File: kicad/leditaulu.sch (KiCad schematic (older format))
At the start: 5 parts

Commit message: Continue schematic
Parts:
- added AFF1: Display 1, symbol LDS-30102BX
- added AFF2: Display 2, symbol LDS-30102BX
- added C2, C? (x2): 10uF, symbol C_Small
- added C? (x2): 1000uF, symbol C_Small
- added C?: 100uF, symbol C_Small
- added CON1: 12V input, symbol BARREL_JACK
- added P2: I2C addr select, symbol CONN_02X04
- added P?: Interconnect, symbol CONN_01X05
- added R1, R11, R2, R3, R6, R7, R8, R9: 10K, symbol R_Small
- added R10: 1K, symbol R_Small
- added U2: TLC59116IPWR, symbol TLC59116IPWR
- added U3: LD1086, SOT-223, symbol LD1117S12CTR
- gave numbers to parts that had none: 5
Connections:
- net 3V3: now also C2.2, C?.1, C?.1, C?.1, P?.2 (P2), R1.1, R11.2, R2.2, R3.2, R6.2, R7.2, R8.2, R9.2, U2.28 (VCC), U3.2 (VO); no longer U1.3 (CH_PD)
- net Earth: now also C2.1, C?.2, C?.2, C?.2, C?.2, C?.2, CON1.2, P2.1 (P1), P2.3 (P3), P2.5 (P5), P2.7 (P7), P?.5 (P5), R10.2, U2.10 (GND), U2.19 (GND), U2.24 (GND), U3.1 (GND)
- net SCL: now also P?.3 (P3), R2.1, U2.26 (SCL)
- net SDA: now also P?.4 (P4), R3.1, U2.27 (SDA)
- new net: R1.2, U1.3 (CH_PD)
- new net: R10.1, U2.1 (REXT)
- new net: AFF1.4 (c), U2.11 (OUT4)
- new net: AFF1.6 (b), U2.12 (OUT5)
- new net: AFF1.7 (a), U2.13 (OUT6)
- new net: AFF1.8 (DP), U2.14 (OUT7)
- new net: AFF2.10 (g), U2.15 (OUT8)
- new net: AFF2.9 (f), U2.16 (OUT9)
- new net: AFF2.2 (e), U2.17 (OUT10)
- new net: AFF2.3 (d), U2.18 (OUT11)
- new net: P2.2 (P2), R6.1, U2.2 (A0)
- new net: AFF2.4 (c), U2.20 (OUT12)
- new net: AFF2.6 (b), U2.21 (OUT13)
- new net: AFF2.7 (a), U2.22 (OUT14)
- new net: AFF2.8 (DP), U2.23 (OUT15)
- new net: R11.1, U2.25 (RESET)
- new net: P2.4 (P4), R7.1, U2.3 (A1)
- new net: P2.6 (P6), R8.1, U2.4 (A2)
- new net: P2.8 (P8), R9.1, U2.5 (A3)
- new net: AFF1.10 (g), U2.6 (OUT0)
- new net: AFF1.9 (f), U2.7 (OUT1)
- new net: AFF1.2 (e), U2.8 (OUT2)
- new net: AFF1.3 (d), U2.9 (OUT3)
- new net VCC: AFF1.1 (C.A.), AFF1.5 (C.A.), AFF2.1 (C.A.), AFF2.5 (C.A.), C?.1, C?.1, CON1.1, P?.1 (P1), U3.3 (VI)
- no-connect marks 7 -> 8
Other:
- moved on the sheet: C1, P1, R4, R5, U1

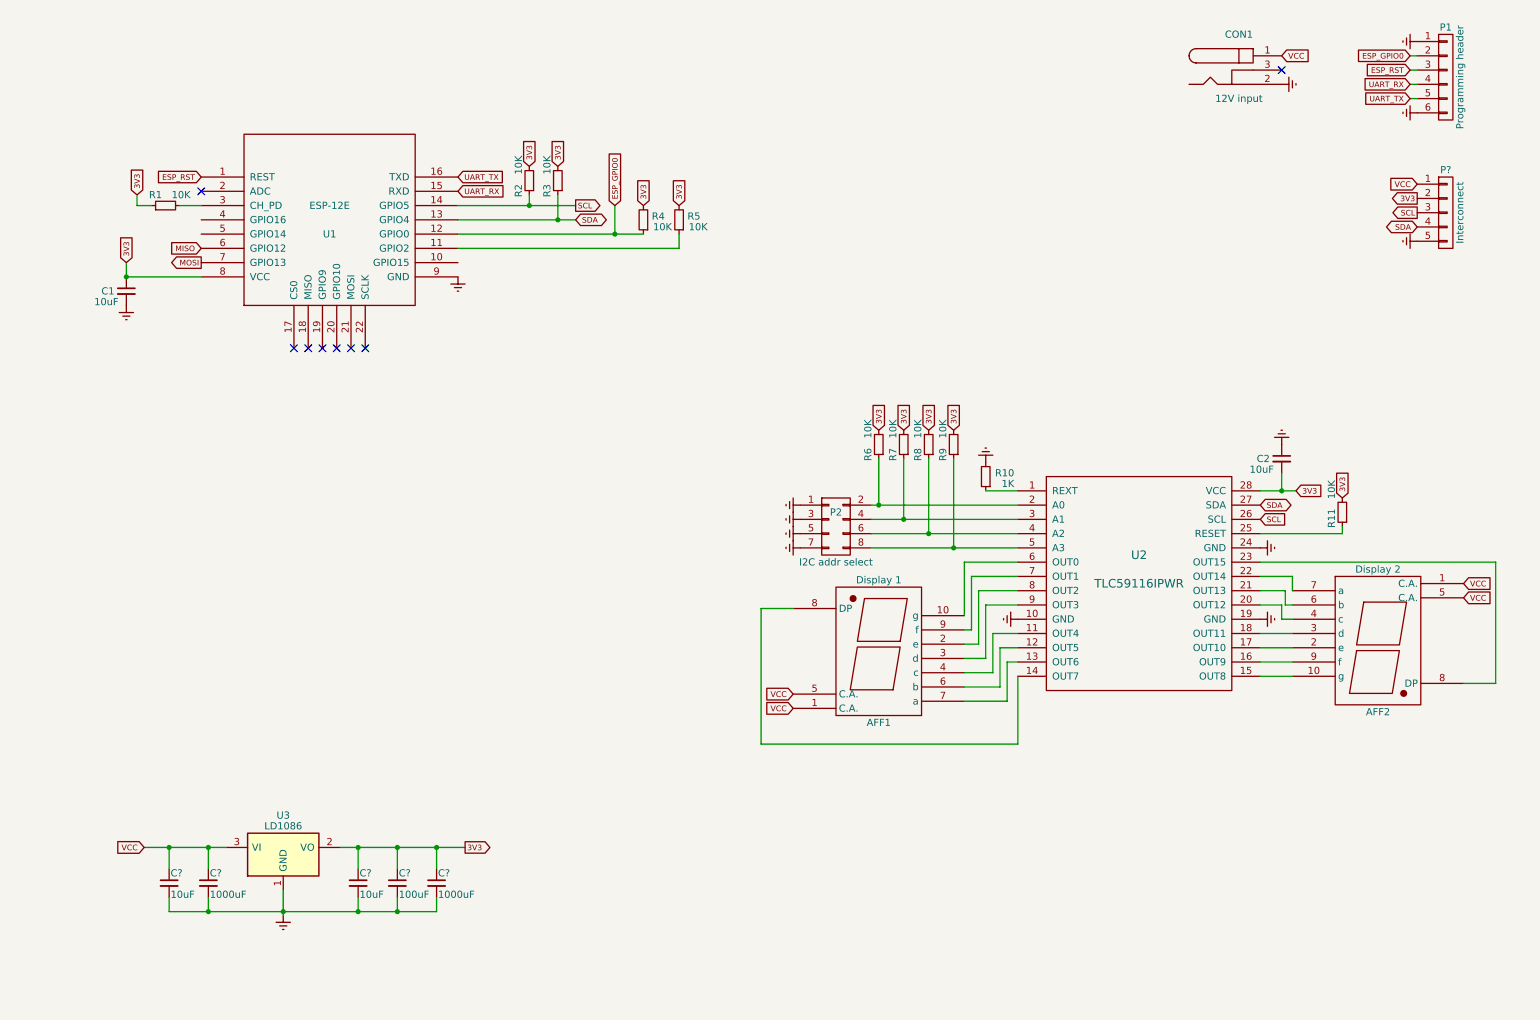
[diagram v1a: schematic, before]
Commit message: Add nRF24L01+
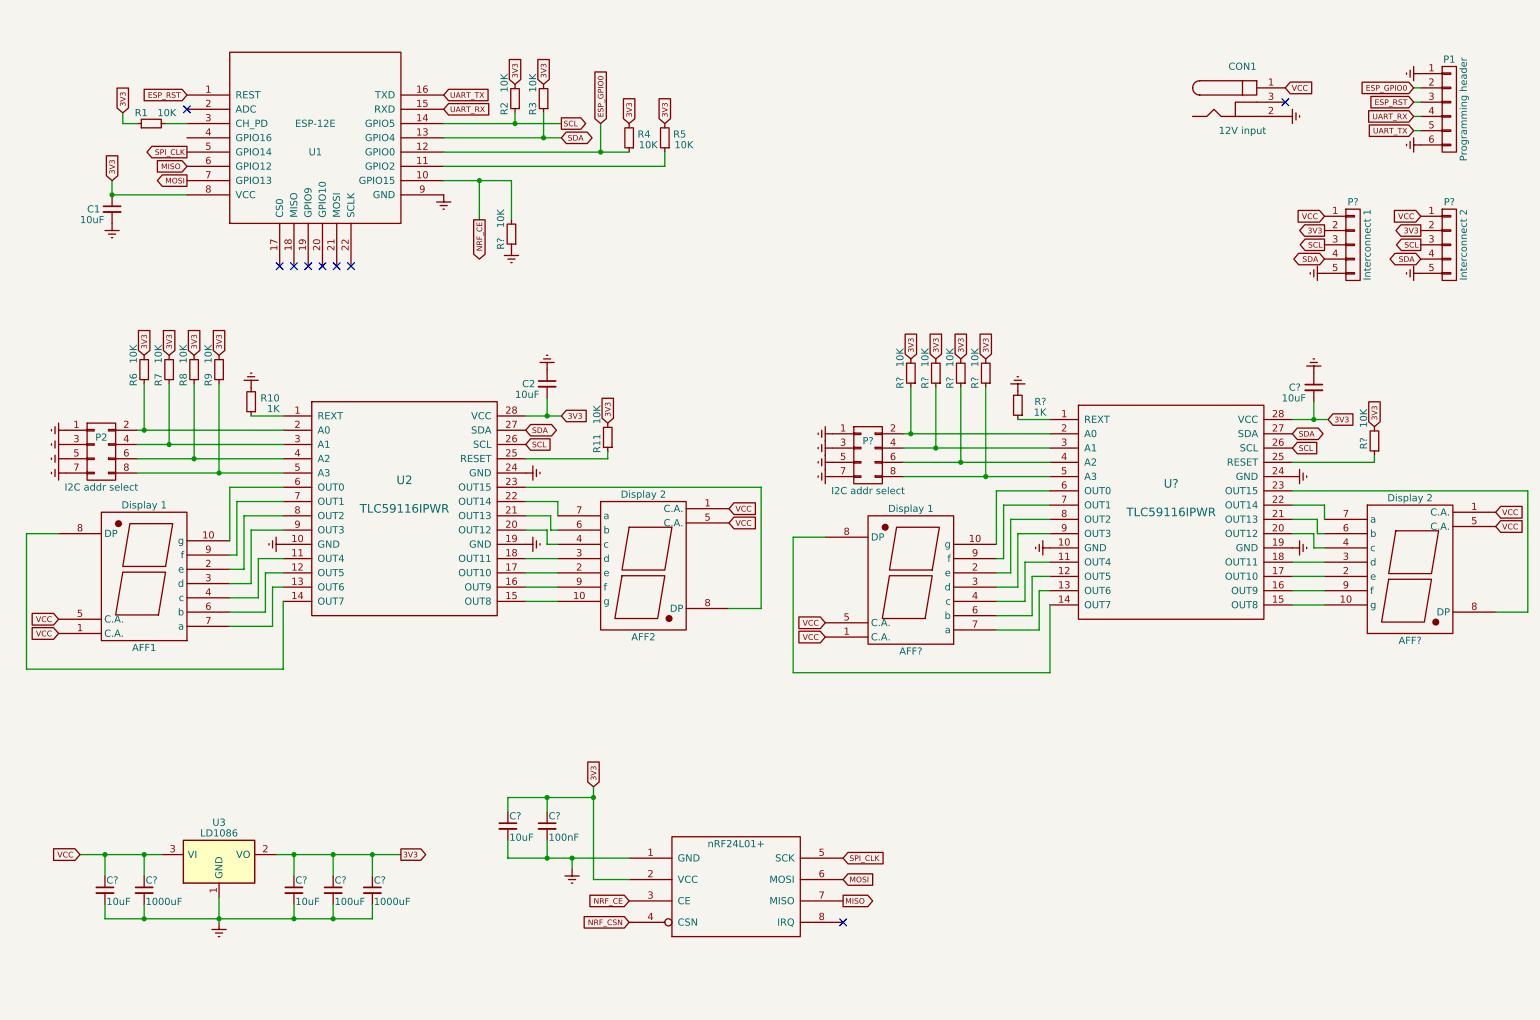
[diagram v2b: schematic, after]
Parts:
- added AFF?: Display 2, symbol LDS-30102BX
- added AFF?: Display 1, symbol LDS-30102BX
- added C? (x2): 10uF, symbol C_Small
- added C?: 100nF, symbol C_Small
- added P?: Interconnect 1, symbol CONN_01X05
- added P?: I2C addr select, symbol CONN_02X04
- added R?: 1K, symbol R_Small
- added R? (x6): 10K, symbol R_Small
- added U?: nRF24L01+, MODULE, symbol nRF24L01+
- added U?: TLC59116IPWR, symbol TLC59116IPWR
- P?: value Interconnect -> Interconnect 2
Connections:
- net 3V3: now also C?.1, C?.1, C?.2, P?.2 (P2), R?.2, R?.2, R?.2, R?.2, R?.2, U?.2 (VCC), U?.28 (VCC)
- net Earth: now also C?.1, C?.2, C?.2, P?.1 (P1), P?.3 (P3), P?.5 (P5), P?.5 (P5), P?.7 (P7), R?.1, R?.2, U?.1 (GND), U?.10 (GND), U?.19 (GND), U?.24 (GND)
- net MISO: now also U?.7 (MISO)
- net MOSI: now also U?.6 (MOSI)
- net SCL: now also P?.3 (P3), U?.26 (SCL)
- net SDA: now also P?.4 (P4), U?.27 (SDA)
- net VCC: now also AFF?.1 (C.A.), AFF?.1 (C.A.), AFF?.5 (C.A.), AFF?.5 (C.A.), P?.1 (P1)
- net NRF_CE: now reaches U1.10 (GPIO15)
- net NRF_CE: now also R?.2, U?.3 (CE)
- net SPI_CLK: now reaches U1.5 (GPIO14)
- net SPI_CLK: now also U?.5 (SCK)
- new net: R?.1, U?.1 (REXT)
- new net: AFF?.4 (c), U?.11 (OUT4)
- new net: AFF?.6 (b), U?.12 (OUT5)
- new net: AFF?.7 (a), U?.13 (OUT6)
- new net: AFF?.8 (DP), U?.14 (OUT7)
- new net: AFF?.10 (g), U?.15 (OUT8)
- new net: AFF?.9 (f), U?.16 (OUT9)
- new net: AFF?.2 (e), U?.17 (OUT10)
- new net: AFF?.3 (d), U?.18 (OUT11)
- new net: P?.2 (P2), R?.1, U?.2 (A0)
- new net: AFF?.4 (c), U?.20 (OUT12)
- new net: AFF?.6 (b), U?.21 (OUT13)
- new net: AFF?.7 (a), U?.22 (OUT14)
- new net: AFF?.8 (DP), U?.23 (OUT15)
- new net: R?.1, U?.25 (RESET)
- new net: P?.4 (P4), R?.1, U?.3 (A1)
- new net: P?.6 (P6), R?.1, U?.4 (A2)
- new net: P?.8 (P8), R?.1, U?.5 (A3)
- new net: AFF?.10 (g), U?.6 (OUT0)
- new net: AFF?.9 (f), U?.7 (OUT1)
- new net: AFF?.2 (e), U?.8 (OUT2)
- new net: AFF?.3 (d), U?.9 (OUT3)
- new net NRF_CSN: U?.4 (CSN)
- no-connect marks 8 -> 9
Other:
- moved on the sheet: AFF1, AFF2, C1, C2, C?, CON1, P1, P2, P?, R1, R10, R11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

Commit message: Finish schematic and footprint associations
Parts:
- AFF1, AFF2: footprint (none) -> Connect:IDC_Header_Straight_10pins
- AFF3, AFF4: renamed from AFF?; footprint (none) -> Connect:IDC_Header_Straight_10pins
- C1, C2: footprint (none) -> Capacitors_SMD:C_1206_HandSoldering
- C10, C3, C5, C6, C8, C9: renamed from C?; footprint (none) -> Capacitors_SMD:C_1206_HandSoldering
- C4, C7: renamed from C?; footprint (none) -> Capacitors_ThroughHole:CP_Radial_D10.0mm_P5.00mm
- CON1: footprint (none) -> Connect:BARREL_JACK
- P1: footprint (none) -> Pin_Headers:Pin_Header_Straight_2x03_Pitch2.54mm
- P2: footprint (none) -> Pin_Headers:Pin_Header_Straight_2x04_Pitch2.54mm
- P4: renamed from P?; footprint (none) -> Pin_Headers:Pin_Header_Straight_2x04_Pitch2.54mm
- P5, P6: renamed from P?; footprint (none) -> Pin_Headers:Pin_Header_Straight_1x05_Pitch2.54mm
- R1, R10, R11, R2, R3, R4, R5, R6, R7, R8, R9: footprint (none) -> Resistors_SMD:R_1206_HandSoldering
- R12, R13, R14, R15, R16, R17, R18: renamed from R?; footprint (none) -> Resistors_SMD:R_1206_HandSoldering
- U1: footprint (none) -> ESP8266:ESP-12E
- U2: footprint (none) -> Housings_SSOP:TSSOP-28_4.4x9.7mm_Pitch0.65mm
- U3: footprint SOT-223 -> TO_SOT_Packages_SMD:TO-263-3Lead
- U4: renamed from U?; footprint MODULE -> mysensors_radios:NRF24L01
- U5: renamed from U?; footprint (none) -> Housings_SSOP:TSSOP-28_4.4x9.7mm_Pitch0.65mm
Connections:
- net NRF_CSN: now also R5.1, U1.11 (GPIO2)
- no-connect marks 9 -> 10

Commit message: Start routing
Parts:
- AFF3: value Display 1 -> Display 3
- AFF4: value Display 2 -> Display 4
- P1: footprint Pin_Headers:Pin_Header_Straight_2x03_Pitch2.54mm -> Pin_Headers:Pin_Header_Straight_1x06_Pitch2.54mm
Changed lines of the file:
@@
 F 0 "P1" H 10575 1600 50  0000 C CNN
 F 1 "Programming header" V 10675 1250 50  0000 C CNN
-F 2 "Pin_Headers:Pin_Header_Straight_2x03_Pitch2.54mm" H 10575 1250 50  0001 C CNN
+F 2 "Pin_Headers:Pin_Header_Straight_1x06_Pitch2.54mm" H 10575 1250 50  0001 C CNN
 F 3 "" H 10575 1250 50  0000 C CNN
 	1    10575 1250
@@
 P 10300 4525
 F 0 "AFF4" H 10300 4075 50  0000 C CNN
-F 1 "Display 2" H 10300 5075 50  0000 C CNN
+F 1 "Display 4" H 10300 5075 50  0000 C CNN
 F 2 "Connect:IDC_Header_Straight_10pins" H 10300 4525 50  0001 C CNN
 F 3 "" H 10300 4525 50  0000 C CNN
@@
 P 6800 4500
 F 0 "AFF3" H 6800 5050 50  0000 C CNN
-F 1 "Display 1" H 6800 4050 50  0000 C CNN
+F 1 "Display 3" H 6800 4050 50  0000 C CNN
 F 2 "Connect:IDC_Header_Straight_10pins" H 6800 4500 50  0001 C CNN
 F 3 "" H 6800 4500 50  0000 C CNN

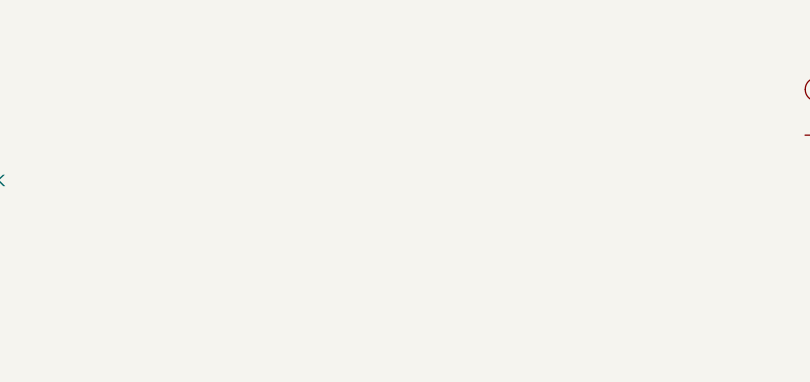
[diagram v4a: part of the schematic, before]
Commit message: Add buttons, continue routing
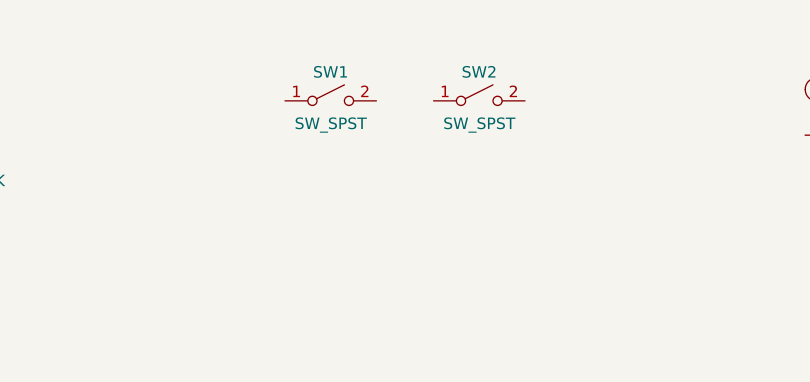
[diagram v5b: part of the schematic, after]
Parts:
- added SW1, SW2: SW_SPST, symbol SW_SPST
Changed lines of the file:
@@
 LIBS:lds-30102bx
 LIBS:nrf24l01+
+LIBS:switches
 LIBS:leditaulu-cache
 EELAYER 25 0
@@
 ESP_GPIO0
 $Comp
-L Earth #PWR01
+L Earth #PWR26
 U 1 1 58EA62EF
 P 10375 1000
-F 0 "#PWR01" H 10375 750 50  0001 C CNN
+F 0 "#PWR26" H 10375 750 50  0001 C CNN
 F 1 "Earth" H 10375 850 50  0001 C CNN
 F 2 "" H 10375 1000 50  0000 C CNN
@@
 $EndComp
 $Comp
-L Earth #PWR02
+L Earth #PWR27
 U 1 1 58EA6329
 P 10375 1500
-F 0 "#PWR02" H 10375 1250 50  0001 C CNN
+F 0 "#PWR27" H 10375 1250 50  0001 C CNN
 F 1 "Earth" H 10375 1350 50  0001 C CNN
 F 2 "" H 10375 1500 50  0000 C CNN
@@
 3V3
 $Comp
-L Earth #PWR03
+L Earth #PWR9
 U 1 1 58EA6BBD
 P 3525 1850
-F 0 "#PWR03" H 3525 1600 50  0001 C CNN
+F 0 "#PWR9" H 3525 1600 50  0001 C CNN
 F 1 "Earth" H 3525 1700 50  0001 C CNN
 F 2 "" H 3525 1850 50  0000 C CNN
@@
 $EndComp
 $Comp
-L Earth #PWR04
+L Earth #PWR5
 U 1 1 58EA6CA7
 P 1200 2050
-F 0 "#PWR04" H 1200 1800 50  0001 C CNN
+F 0 "#PWR5" H 1200 1800 50  0001 C CNN
 F 1 "Earth" H 1200 1900 50  0001 C CNN
 F 2 "" H 1200 2050 50  0000 C CNN
@@
 $EndComp
 $Comp
-L Earth #PWR05
+L Earth #PWR8
 U 1 1 58EBE920
 P 2400 4300
-F 0 "#PWR05" H 2400 4050 50  0001 C CNN
+F 0 "#PWR8" H 2400 4050 50  0001 C CNN
 F 1 "Earth" H 2400 4150 50  0001 C CNN
 F 2 "" H 2400 4300 50  0000 C CNN
@@
 $EndComp
 $Comp
-L Earth #PWR06
+L Earth #PWR11
 U 1 1 58EBE9BE
 P 4100 3800
-F 0 "#PWR06" H 4100 3550 50  0001 C CNN
+F 0 "#PWR11" H 4100 3550 50  0001 C CNN
 F 1 "Earth" H 4100 3650 50  0001 C CNN
 F 2 "" H 4100 3800 50  0000 C CNN
@@
 $EndComp
 $Comp
-L Earth #PWR07
+L Earth #PWR12
 U 1 1 58EBE9F7
 P 4100 4300
-F 0 "#PWR07" H 4100 4050 50  0001 C CNN
+F 0 "#PWR12" H 4100 4050 50  0001 C CNN
 F 1 "Earth" H 4100 4150 50  0001 C CNN
 F 2 "" H 4100 4300 50  0000 C CNN
@@
 $EndComp
 $Comp
-L Earth #PWR08
+L Earth #PWR13
 U 1 1 58EBEB42
 P 4250 3075
-F 0 "#PWR08" H 4250 2825 50  0001 C CNN
+F 0 "#PWR13" H 4250 2825 50  0001 C CNN
 F 1 "Earth" H 4250 2925 50  0001 C CNN
 F 2 "" H 4250 3075 50  0000 C CNN
@@
 $EndComp
 $Comp
-L Earth #PWR09
+L Earth #PWR7
 U 1 1 58EBECB7
 P 2175 3200
-F 0 "#PWR09" H 2175 2950 50  0001 C CNN
+F 0 "#PWR7" H 2175 2950 50  0001 C CNN
 F 1 "Earth" H 2175 3050 50  0001 C CNN
 F 2 "" H 2175 3200 50  0000 C CNN
@@
 3V3
 $Comp
-L Earth #PWR010
+L Earth #PWR1
 U 1 1 58EBF732
 P 875 3500
-F 0 "#PWR010" H 875 3250 50  0001 C CNN
+F 0 "#PWR1" H 875 3250 50  0001 C CNN
 F 1 "Earth" H 875 3350 50  0001 C CNN
 F 2 "" H 875 3500 50  0000 C CNN
@@
 $EndComp
 $Comp
-L Earth #PWR011
+L Earth #PWR2
 U 1 1 58EBF764
 P 875 3600
-F 0 "#PWR011" H 875 3350 50  0001 C CNN
+F 0 "#PWR2" H 875 3350 50  0001 C CNN
 F 1 "Earth" H 875 3450 50  0001 C CNN
 F 2 "" H 875 3600 50  0000 C CNN
@@
 $EndComp
 $Comp
-L Earth #PWR012
+L Earth #PWR3
 U 1 1 58EBF796
 P 875 3700
-F 0 "#PWR012" H 875 3450 50  0001 C CNN
+F 0 "#PWR3" H 875 3450 50  0001 C CNN
 F 1 "Earth" H 875 3550 50  0001 C CNN
 F 2 "" H 875 3700 50  0000 C CNN
@@
 $EndComp
 $Comp
-L Earth #PWR013
+L Earth #PWR4
 U 1 1 58EBF7C8
 P 875 3800
-F 0 "#PWR013" H 875 3550 50  0001 C CNN
+F 0 "#PWR4" H 875 3550 50  0001 C CNN
 F 1 "Earth" H 875 3650 50  0001 C CNN
 F 2 "" H 875 3800 50  0000 C CNN
@@
 3V3
 $Comp
-L Earth #PWR014
+L Earth #PWR6
 U 1 1 58EC372D
 P 1950 6950
-F 0 "#PWR014" H 1950 6700 50  0001 C CNN
+F 0 "#PWR6" H 1950 6700 50  0001 C CNN
 F 1 "Earth" H 1950 6800 50  0001 C CNN
 F 2 "" H 1950 6950 50  0000 C CNN
@@
 VCC
 $Comp
-L Earth #PWR015
+L Earth #PWR21
 U 1 1 58EC41D8
 P 9425 1300
-F 0 "#PWR015" H 9425 1050 50  0001 C CNN
+F 0 "#PWR21" H 9425 1050 50  0001 C CNN
 F 1 "Earth" H 9425 1150 50  0001 C CNN
 F 2 "" H 9425 1300 50  0000 C CNN
@@
 $EndComp
 $Comp
-L Earth #PWR016
+L Earth #PWR28
 U 1 1 58EC54A0
 P 10375 2400
-F 0 "#PWR016" H 10375 2150 50  0001 C CNN
+F 0 "#PWR28" H 10375 2150 50  0001 C CNN
 F 1 "Earth" H 10375 2250 50  0001 C CNN
 F 2 "" H 10375 2400 50  0000 C CNN
@@
 $EndComp
 $Comp
-L Earth #PWR017
+L Earth #PWR25
 U 1 1 58ECFC8A
 P 9700 2400
-F 0 "#PWR017" H 9700 2150 50  0001 C CNN
+F 0 "#PWR25" H 9700 2150 50  0001 C CNN
 F 1 "Earth" H 9700 2250 50  0001 C CNN
 F 2 "" H 9700 2400 50  0000 C CNN
@@
 $EndComp
 $Comp
-L Earth #PWR018
+L Earth #PWR20
 U 1 1 58ED1380
 P 7775 4325
-F 0 "#PWR018" H 7775 4075 50  0001 C CNN
+F 0 "#PWR20" H 7775 4075 50  0001 C CNN
 F 1 "Earth" H 7775 4175 50  0001 C CNN
 F 2 "" H 7775 4325 50  0000 C CNN
@@
 $EndComp
 $Comp
-L Earth #PWR019
+L Earth #PWR22
 U 1 1 58ED1386
 P 9475 3825
-F 0 "#PWR019" H 9475 3575 50  0001 C CNN
+F 0 "#PWR22" H 9475 3575 50  0001 C CNN
 F 1 "Earth" H 9475 3675 50  0001 C CNN
 F 2 "" H 9475 3825 50  0000 C CNN
@@
 $EndComp
 $Comp
-L Earth #PWR020
+L Earth #PWR23
 U 1 1 58ED138C
 P 9475 4325
-F 0 "#PWR020" H 9475 4075 50  0001 C CNN
+F 0 "#PWR23" H 9475 4075 50  0001 C CNN
 F 1 "Earth" H 9475 4175 50  0001 C CNN
 F 2 "" H 9475 4325 50  0000 C CNN
@@
 $EndComp
 $Comp
-L Earth #PWR021
+L Earth #PWR24
 U 1 1 58ED1399
 P 9625 3100
-F 0 "#PWR021" H 9625 2850 50  0001 C CNN
+F 0 "#PWR24" H 9625 2850 50  0001 C CNN
 F 1 "Earth" H 9625 2950 50  0001 C CNN
 F 2 "" H 9625 3100 50  0000 C CNN
@@
 $EndComp
 $Comp
-L Earth #PWR022
+L Earth #PWR19
 U 1 1 58ED13A5
 P 7550 3225
-F 0 "#PWR022" H 7550 2975 50  0001 C CNN
+F 0 "#PWR19" H 7550 2975 50  0001 C CNN
 F 1 "Earth" H 7550 3075 50  0001 C CNN
 F 2 "" H 7550 3225 50  0000 C CNN
@@
 3V3
 $Comp
-L Earth #PWR023
+L Earth #PWR15
 U 1 1 58ED13CD
 P 6250 3525
-F 0 "#PWR023" H 6250 3275 50  0001 C CNN
+F 0 "#PWR15" H 6250 3275 50  0001 C CNN
 F 1 "Earth" H 6250 3375 50  0001 C CNN
 F 2 "" H 6250 3525 50  0000 C CNN
@@
 $EndComp
 $Comp
-L Earth #PWR024
+L Earth #PWR16
 U 1 1 58ED13D3
 P 6250 3625
-F 0 "#PWR024" H 6250 3375 50  0001 C CNN
+F 0 "#PWR16" H 6250 3375 50  0001 C CNN
 F 1 "Earth" H 6250 3475 50  0001 C CNN
 F 2 "" H 6250 3625 50  0000 C CNN
@@
 $EndComp
 $Comp
-L Earth #PWR025
+L Earth #PWR17
 U 1 1 58ED13D9
 P 6250 3725
-F 0 "#PWR025" H 6250 3475 50  0001 C CNN
+F 0 "#PWR17" H 6250 3475 50  0001 C CNN
 F 1 "Earth" H 6250 3575 50  0001 C CNN
 F 2 "" H 6250 3725 50  0000 C CNN
@@
 $EndComp
 $Comp
-L Earth #PWR026
+L Earth #PWR18
 U 1 1 58ED13DF
 P 6250 3825
-F 0 "#PWR026" H 6250 3575 50  0001 C CNN
+F 0 "#PWR18" H 6250 3575 50  0001 C CNN
 F 1 "Earth" H 6250 3675 50  0001 C CNN
 F 2 "" H 6250 3825 50  0000 C CNN
@@
 $EndComp
 $Comp
-L Earth #PWR027
+L Earth #PWR14
 U 1 1 58ED076D
 P 4250 6575
-F 0 "#PWR027" H 4250 6325 50  0001 C CNN
+F 0 "#PWR14" H 4250 6325 50  0001 C CNN
 F 1 "Earth" H 4250 6425 50  0001 C CNN
 F 2 "" H 4250 6575 50  0000 C CNN
@@
 $EndComp
 $Comp
-L Earth #PWR028
+L Earth #PWR10
 U 1 1 58ED6D4A
 P 4000 2225
-F 0 "#PWR028" H 4000 1975 50  0001 C CNN
+F 0 "#PWR10" H 4000 1975 50  0001 C CNN
 F 1 "Earth" H 4000 2075 50  0001 C CNN
 F 2 "" H 4000 2225 50  0000 C CNN
@@
 NoConn ~ 1725 1450
 $Comp
-L PWR_FLAG #FLG029
+L PWR_FLAG #FLG2
 U 1 1 5902A362
 P 1150 6925
-F 0 "#FLG029" H 1150 7020 50  0001 C CNN
+F 0 "#FLG2" H 1150 7020 50  0001 C CNN
 F 1 "PWR_FLAG" H 1150 7105 50  0000 C CNN
 F 2 "" H 1150 6925 50  0000 C CNN
@@
 $EndComp
 $Comp
-L PWR_FLAG #FLG030
+L PWR_FLAG #FLG1
 U 1 1 5902A2A8
 P 1150 6475
-F 0 "#FLG030" H 1150 6570 50  0001 C CNN
+F 0 "#FLG1" H 1150 6570 50  0001 C CNN
 F 1 "PWR_FLAG" H 1150 6655 50  0000 C CNN
 F 2 "" H 1150 6475 50  0000 C CNN
@@
 	1    0    0    -1
 $EndComp
+$Comp
+L SW_SPST SW1
+U 1 1 59036142
+P 6700 1150
+F 0 "SW1" H 6700 1275 50  0000 C CNN
+F 1 "SW_SPST" H 6700 1050 50  0000 C CNN
+F 2 "" H 6700 1150 50  0000 C CNN
+F 3 "" H 6700 1150 50  0000 C CNN
+	1    6700 1150
+	1    0    0    -1
+$EndComp
+$Comp
+L SW_SPST SW2
+U 1 1 590363A7
+P 7350 1150
+F 0 "SW2" H 7350 1275 50  0000 C CNN
+F 1 "SW_SPST" H 7350 1050 50  0000 C CNN
+F 2 "" H 7350 1150 50  0000 C CNN
+F 3 "" H 7350 1150 50  0000 C CNN
+	1    7350 1150
+	1    0    0    -1
+$EndComp
